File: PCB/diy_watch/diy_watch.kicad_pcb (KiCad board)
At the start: 2 copper layers, 35.9 x 36.9 mm, 44 parts, among them IC1 W25Q16JVUXIQ, J1 USB_B_Micro, SW1 SW_Push, U1 FTE-2CA-V-T/R, U2 DS3231MZ, U3 RP2040, U7 XC6210B332MR, U8 LTC4071EMS8E_PBF, Y1 12MHz_crystal

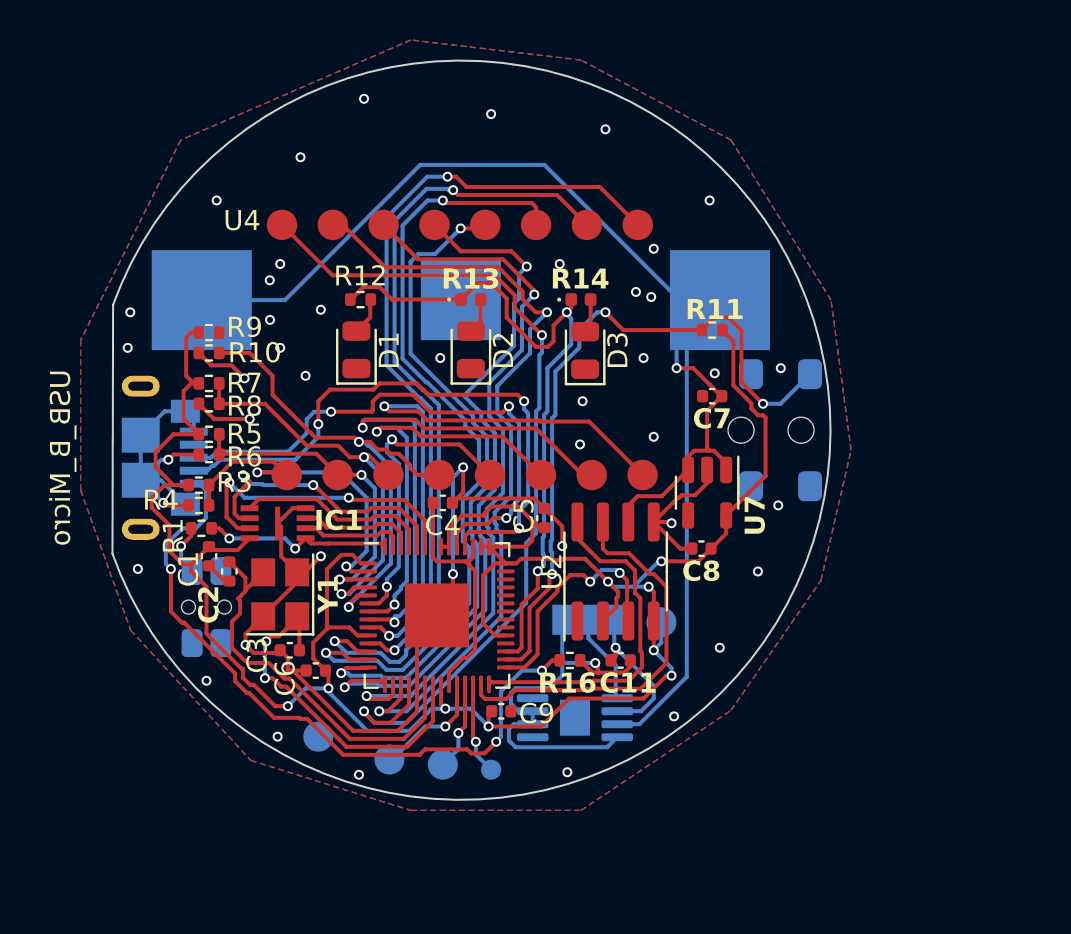
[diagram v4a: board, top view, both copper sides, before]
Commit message: Updating to 4 layer board Adding missing caps to schematic Updating pcb with schematic fixes
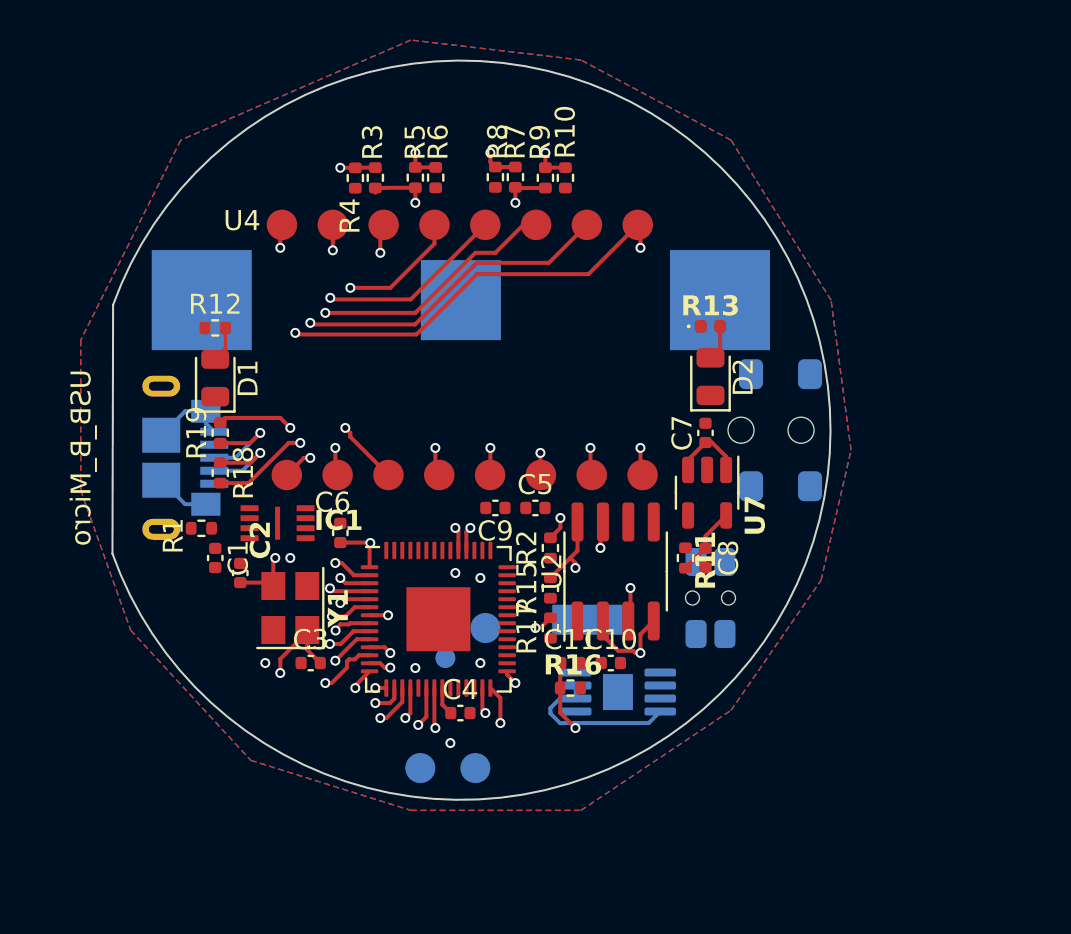
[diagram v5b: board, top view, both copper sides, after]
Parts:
- removed D3: LED, LED_SMD:LED_0805_2012Metric
- removed R14: 300, LED_SMD:LED_0402_1005Metric
- added C10: 1uF, Capacitor_SMD:C_0402_1005Metric, F.Cu at (157.5, 111.6)
- added R15: 10K, Resistor_SMD:R_0402_1005Metric, F.Cu at (154.5, 107.9)
- added R17: 10K, Resistor_SMD:R_0402_1005Metric, F.Cu at (154.5, 109.9)
- added R18: 27R, Resistor_SMD:R_0402_1005Metric, F.Cu at (138.0, 102.1)
- added R19: 27R, Resistor_SMD:R_0402_1005Metric, F.Cu at (138.0, 100.1)
- added R2: 10K, Resistor_SMD:R_0402_1005Metric, F.Cu at (154.5, 105.9)
- C11: value 1uf -> 1uF
- moved SW1 25.2 mm to (162.5, 108.4), turned to -90 degrees
- moved R10 19.8 mm to (155.2, 87.4), turned to -90 degrees
- moved R9 18.5 mm to (154.2, 87.4), turned to 90 degrees
- moved R7 18.5 mm to (152.7, 87.4), turned to 90 degrees
- moved R8 18.2 mm to (151.7, 87.4), turned to -90 degrees
- moved R4 18.1 mm to (144.7, 87.4), turned to -90 degrees
- moved R6 17.9 mm to (148.7, 87.4), turned to -90 degrees
- moved R3 17.7 mm to (145.7, 87.4), turned to 90 degrees
- moved R5 16.5 mm to (147.7, 87.4), turned to 90 degrees
- moved D2 12.0 mm to (162.5, 97.3)
- moved R13 12.0 mm to (162.5, 94.8)
- moved TP5 11.8 mm to (150.7, 116.9)
- moved R11 11.5 mm to (161.2, 106.4), turned to 90 degrees
- moved C4 10.5 mm to (150.0, 114.1)
- moved C9 10.2 mm to (151.7, 103.9), turned to 180 degrees
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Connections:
- C11 pad 1: Net-(JP1-B) -> VCC
- C4 pad 1: +1V1 -> +3.3V
- C5 pad 1: +3.3V -> +1V1
- C7 pad 1: +BATT -> VCC
- JP1 pad 3: Net-(JP1-B) -> VCC
- R16 pad 2: Net-(JP1-B) -> VCC
- U3 pad 46: /usb_D- -> /USB_DMX
- U3 pad 47: /usb_D+ -> /USB_DPX
- U7 pad 1: +BATT -> VCC
- U7 pad 3: +BATT -> VCC
- U8 pad 2: Net-(JP1-B) -> VCC
- U8 pad 3: Net-(JP1-B) -> VCC
- U8 pad 8: Net-(JP1-B) -> VCC
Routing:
- net +3.3V: track 119.5 -> 29.8 mm, vias 9 -> 5
- net GND: track 82.8 -> 6.89 mm, vias 45 -> 7
- net +BATT: track 74.2 -> 0.00 mm, vias 1 -> 0
- net /light_sw: track 35.1 -> 0.00 mm, vias 3 -> 0
- net /light_en: track 34.2 -> 0.00 mm, vias 2 -> 0
- net +5V: track 34.2 -> 0.00 mm, vias 3 -> 0
- net /usb_D-: track 29.7 -> 4.87 mm, vias 3 -> 1
- net /usb_D+: track 27.8 -> 5.02 mm, vias 3 -> 1
- net Net-(JP1-B): track 21.1 -> 0.00 mm, vias 1 -> 0
- net /USB_DMX: track 0.00 -> 17.5 mm, vias 0 -> 2
- net /USB_DPX: track 0.00 -> 16.8 mm, vias 0 -> 2
- net VCC: track 0.00 -> 15.9 mm, vias 0 -> 1
- net Net-(IC1-(IO3)): track 15.0 -> 0.00 mm, vias 2 -> 0
- net Net-(IC1-CLK): track 14.1 -> 0.00 mm, vias 2 -> 0
- net /COM3: track 21.1 -> 35.0 mm, vias 2 -> 3
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- added copper zone on In1.Cu, net GND
- added copper zone on In2.Cu, net GND
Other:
- copper layers 2 -> 4

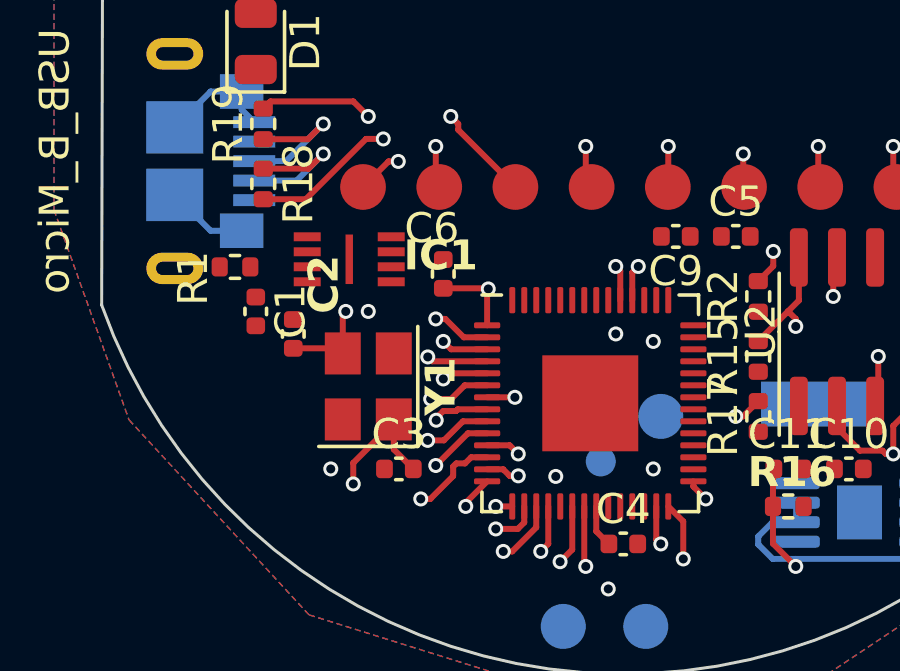
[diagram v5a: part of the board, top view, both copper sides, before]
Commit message: Added more PCB tracks
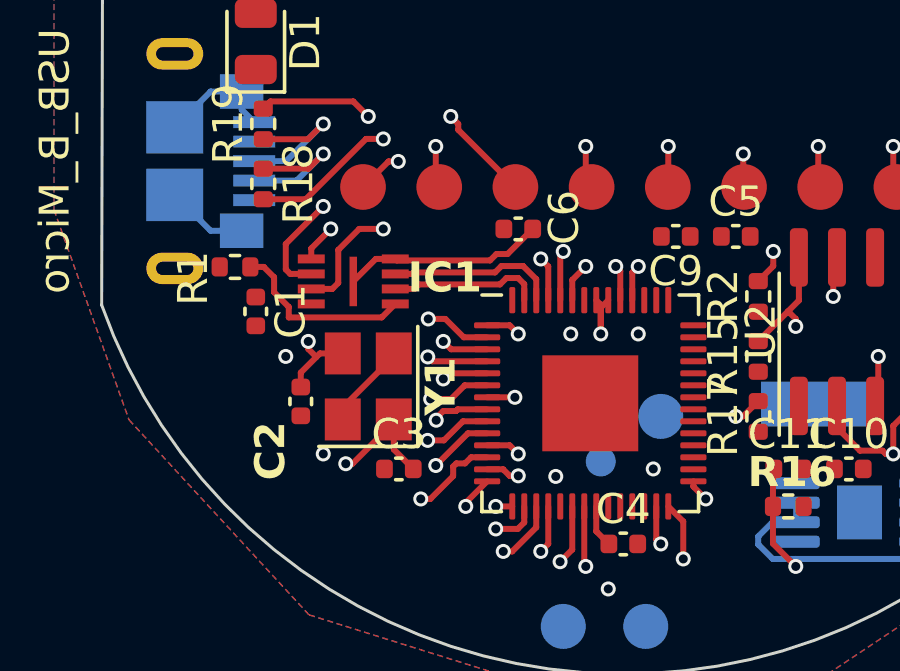
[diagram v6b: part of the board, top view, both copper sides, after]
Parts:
- moved C6 2.92 mm to (146.5, 103.6), turned to 0 degrees
- moved C2 2.26 mm to (139.2, 109.4), turned to 90 degrees
- moved IC1 0.75 mm to (141.0, 105.4)
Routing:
- net Net-(IC1-CLK): track 0.00 -> 14.0 mm, vias 0 -> 2
- net Net-(IC1-(IO3)): track 0.00 -> 12.8 mm, vias 0 -> 2
- net Net-(IC1-DI_(IO0)): track 0.00 -> 10.3 mm, vias 0 -> 2
- net GND: track 6.89 -> 16.6 mm
- net Net-(IC1-~{CS}): track 0.00 -> 6.21 mm
- net Net-(IC1-~{WP_}(IO2)): track 0.00 -> 5.69 mm
- net Net-(IC1-DO_(IO1)): track 0.00 -> 5.07 mm
- net /A: track 16.5 -> 20.8 mm
- net +3.3V: track 29.8 -> 33.9 mm, vias 5 -> 6
- net /G: track 42.2 -> 45.9 mm
- net /F: track 41.2 -> 43.6 mm
- net /E: track 45.0 -> 47.3 mm
- net /H: track 39.2 -> 41.3 mm
- net /L: track 37.6 -> 39.3 mm
- net /K: track 38.0 -> 39.6 mm
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
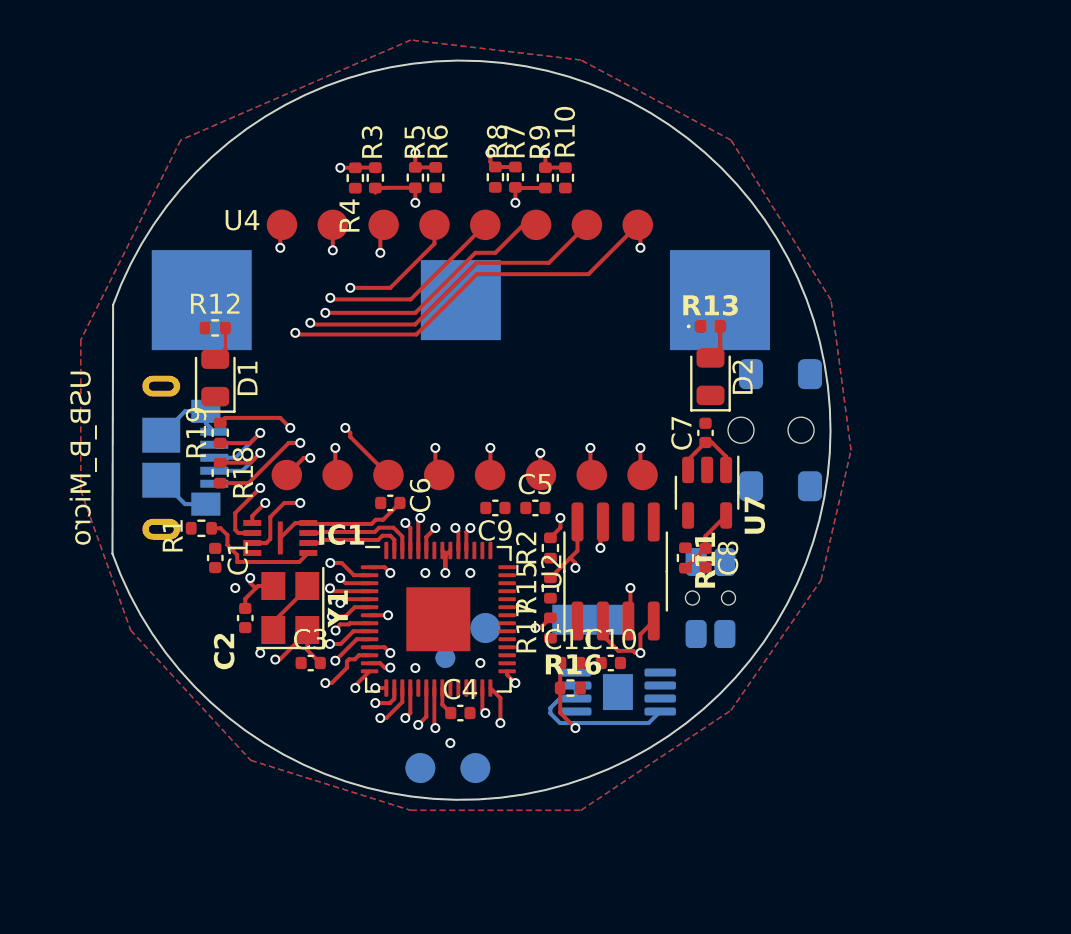
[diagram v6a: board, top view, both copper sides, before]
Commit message: Refactored layer setup to be more efficient
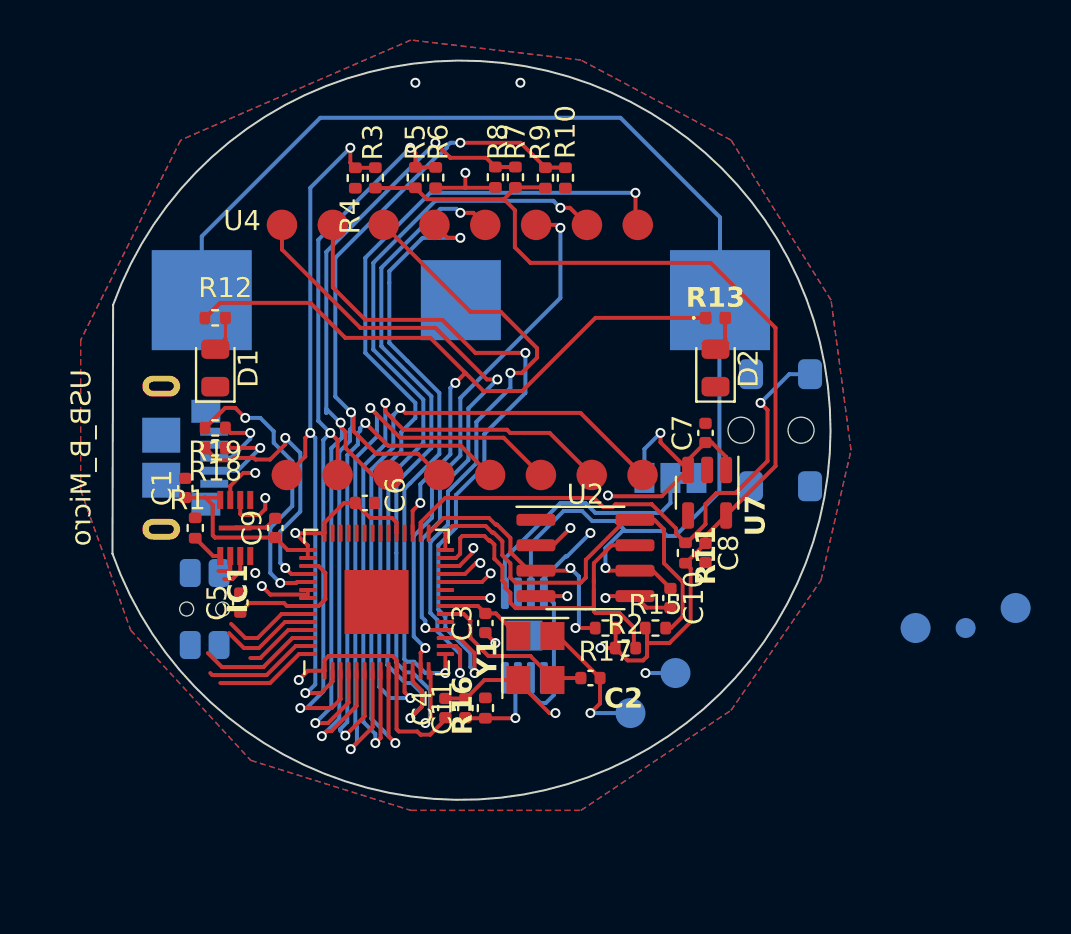
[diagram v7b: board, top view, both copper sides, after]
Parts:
- moved TP3 26.5 mm to (177.7, 108.9)
- moved TP4 26.0 mm to (175.2, 109.9)
- moved SW1 25.3 mm to (137.2, 108.9), turned to 90 degrees
- moved TP1 24.0 mm to (172.7, 109.9)
- moved C2 17.5 mm to (156.5, 112.4), turned to 180 degrees
- moved C5 15.5 mm to (139.0, 108.6), turned to 90 degrees
- moved Y1 12.5 mm to (153.7, 111.4), turned to -90 degrees
- moved TP5 11.1 mm to (160.7, 112.1)
- moved C9 11.0 mm to (140.7, 104.9), turned to 90 degrees
- moved TP2 10.9 mm to (158.5, 114.1)
- moved C3 8.96 mm to (151.2, 109.6), turned to 90 degrees
- moved JP1 8.19 mm to (160.5, 102.4)
- moved R2 6.25 mm to (158.2, 110.9), turned to 0 degrees
- moved C11 5.71 mm to (150.2, 113.9), turned to 90 degrees
- moved R15 5.62 mm to (159.7, 109.9), turned to 0 degrees
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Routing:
- net +3.3V: track 33.9 -> 129.5 mm, vias 6 -> 8
- net +BATT: track 0.00 -> 67.4 mm, vias 0 -> 1
- net /light_en: track 0.00 -> 37.8 mm, vias 0 -> 2
- net /light_sw: track 0.00 -> 28.0 mm, vias 0 -> 1
- net /G: track 45.9 -> 26.8 mm
- net VCC: track 15.9 -> 32.4 mm, vias 1 -> 4
- net /B: track 16.2 -> 32.1 mm
- net Net-(JP1-C): track 0.00 -> 12.8 mm
- net Net-(U3-XOUT): track 16.6 -> 4.39 mm, vias 2 -> 0
- net /C: track 21.7 -> 33.5 mm
- net /COM4: track 38.2 -> 49.6 mm
- net /I: track 40.7 -> 30.2 mm
- net /D: track 24.7 -> 35.1 mm
- net /COM2: track 29.3 -> 38.9 mm
- net /COM3: track 35.3 -> 44.8 mm
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
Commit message: More routing on new 4 layer stack
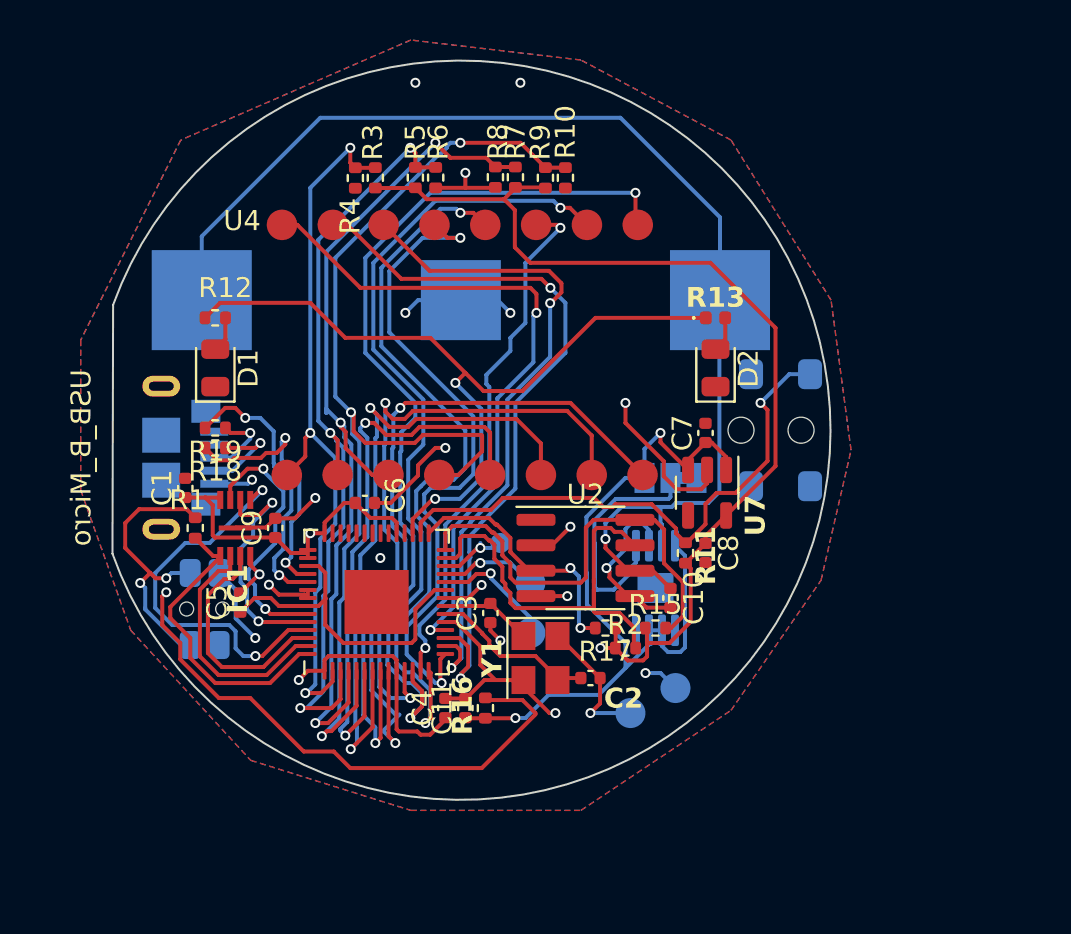
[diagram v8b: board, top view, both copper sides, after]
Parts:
- moved TP3 24.3 mm to (153.5, 107.6)
- moved TP4 23.6 mm to (152.0, 105.6)
- moved TP1 19.3 mm to (153.5, 110.1)
- moved U8 6.97 mm to (159.7, 107.9)
- moved TP5 0.75 mm to (160.7, 112.9)
- moved C3 0.56 mm to (151.5, 109.1)
- moved Y1 0.25 mm to (154.0, 111.4)
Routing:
- net +5V: track 0.00 -> 37.8 mm, vias 0 -> 2
- net GND: track 25.4 -> 62.5 mm, vias 8 -> 15
- net Net-(IC1-DI_(IO0)): track 3.45 -> 19.3 mm, vias 0 -> 2
- net Net-(R1-Pad1): track 0.00 -> 14.3 mm, vias 0 -> 2
- net +1V1: track 6.98 -> 16.9 mm
- net Net-(IC1-~{CS}): track 6.69 -> 15.3 mm
- net VCC: track 32.4 -> 40.3 mm, vias 4 -> 2
- net Net-(IC1-(IO3)): track 6.85 -> 13.4 mm, vias 1 -> 2
- net +BATT: track 67.4 -> 61.0 mm
- net Net-(IC1-DO_(IO1)): track 6.82 -> 12.3 mm
- net /COM4: track 49.6 -> 55.0 mm
- net Net-(IC1-CLK): track 7.43 -> 12.0 mm, vias 1 -> 2
- net /L: track 29.8 -> 33.9 mm
- net Net-(IC1-~{WP_}(IO2)): track 7.61 -> 11.6 mm
- net Net-(U3-SWCLK): track 2.45 -> 6.25 mm
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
